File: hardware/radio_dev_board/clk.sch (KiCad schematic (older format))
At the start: 11 parts

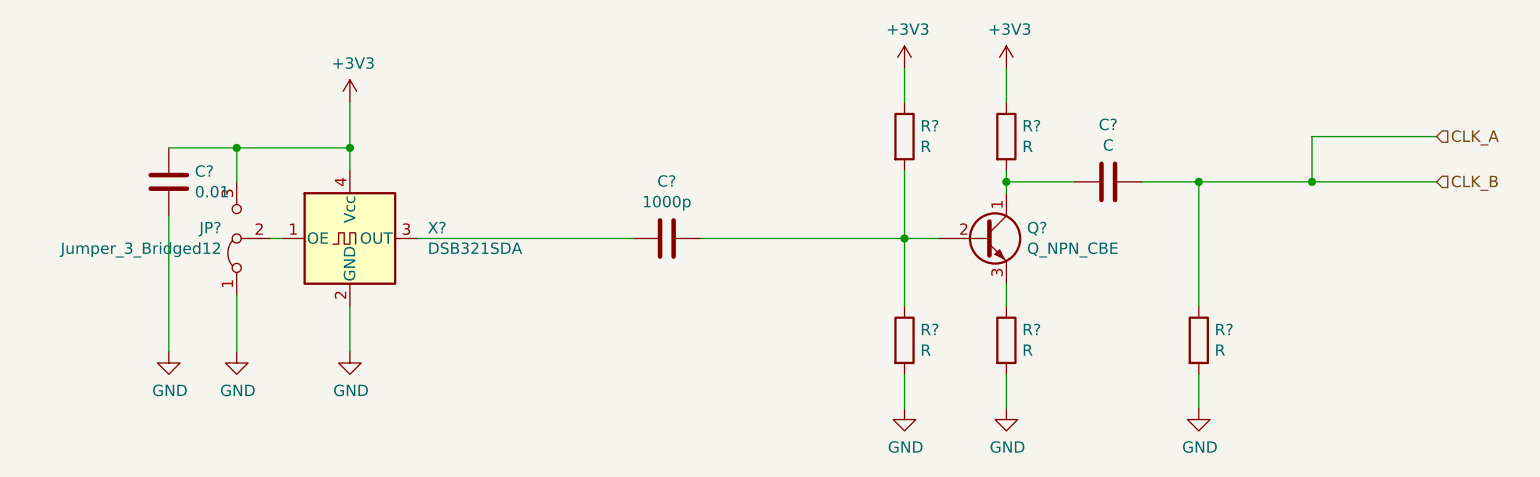
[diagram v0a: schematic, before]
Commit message: added radio USB serial channel. Update board layout
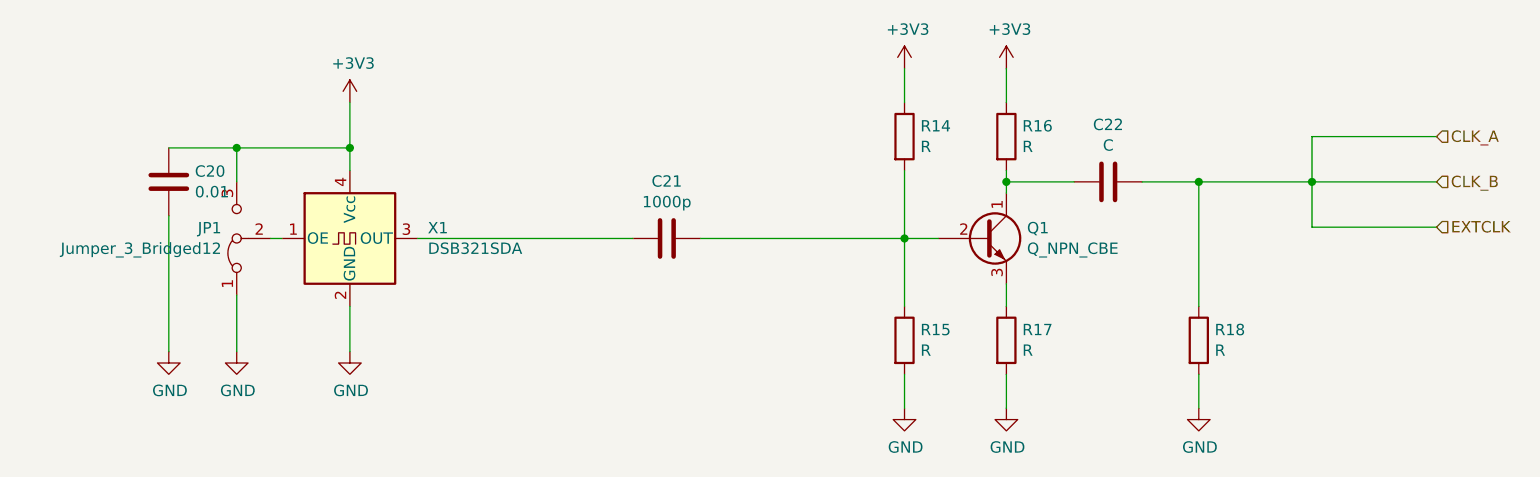
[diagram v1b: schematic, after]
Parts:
- C20, C21, C22: renamed from C?; footprint (none) -> Capacitor_SMD:C_0603_1608Metric_Pad1.05x0.95mm_HandSolder
- JP1: renamed from JP?; footprint (none) -> Jumper:SolderJumper-3_P1.3mm_Bridged2Bar12_Pad1.0x1.5mm
- Q1: renamed from Q?; footprint (none) -> Package_TO_SOT_SMD:SOT-23
- R14, R15, R16, R17, R18: renamed from R?; footprint (none) -> Resistor_SMD:R_0603_1608Metric_Pad1.05x0.95mm_HandSolder
- gave numbers to parts that had none: 1
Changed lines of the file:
@@
 $Descr A4 11693 8268
 encoding utf-8
-Sheet 5 5
+Sheet 5 6
 Title ""
 Date ""
@@
 $EndDescr
 $Comp
-L Oscillator:SG-210SED X?
+L Oscillator:SG-210SED X1
 U 1 1 5DEE1FC3
 P 4550 4050
-F 0 "X?" H 4894 4096 50  0000 L CNN
+F 0 "X1" H 4894 4096 50  0000 L CNN
 F 1 "DSB321SDA" H 4894 4005 50  0000 L CNN
 F 2 "Oscillator:Oscillator_SMD_SeikoEpson_SG210-4Pin_2.5x2.0mm" H 5000 3700 50  0001 C CNN
@@
 $EndComp
 $Comp
-L power:+3V3 #PWR?
+L power:+3V3 #PWR060
 U 1 1 5DEE2566
 P 4550 3450
-F 0 "#PWR?" H 4550 3300 50  0001 C CNN
+F 0 "#PWR060" H 4550 3300 50  0001 C CNN
 F 1 "+3V3" H 4565 3623 50  0000 C CNN
 F 2 "" H 4550 3450 50  0001 C CNN
@@
 $EndComp
 $Comp
-L power:GND #PWR?
+L power:GND #PWR061
 U 1 1 5DEE2C97
 P 4550 4550
-F 0 "#PWR?" H 4550 4300 50  0001 C CNN
+F 0 "#PWR061" H 4550 4300 50  0001 C CNN
 F 1 "GND" H 4555 4377 50  0000 C CNN
 F 2 "" H 4550 4550 50  0001 C CNN
@@
 $EndComp
 $Comp
-L power:GND #PWR?
+L power:GND #PWR059
 U 1 1 5DEE2E7E
 P 4050 4550
-F 0 "#PWR?" H 4050 4300 50  0001 C CNN
+F 0 "#PWR059" H 4050 4300 50  0001 C CNN
 F 1 "GND" H 4055 4377 50  0000 C CNN
 F 2 "" H 4050 4550 50  0001 C CNN
@@
 	4850 4050 5800 4050
 $Comp
-L Device:C C?
+L Device:C C21
 U 1 1 5DEE3315
 P 5950 4050
-F 0 "C?" V 5698 4050 50  0000 C CNN
+F 0 "C21" V 5698 4050 50  0000 C CNN
 F 1 "1000p" V 5789 4050 50  0000 C CNN
-F 2 "" H 5988 3900 50  0001 C CNN
+F 2 "Capacitor_SMD:C_0603_1608Metric_Pad1.05x0.95mm_HandSolder" H 5988 3900 50  0001 C CNN
 F 3 "~" H 5950 4050 50  0001 C CNN
 	1    5950 4050
@@
 $EndComp
 $Comp
-L Device:C C?
+L Device:C C20
 U 1 1 5DEE35E3
 P 3750 3800
-F 0 "C?" H 3865 3846 50  0000 L CNN
+F 0 "C20" H 3865 3846 50  0000 L CNN
 F 1 "0.01" H 3865 3755 50  0000 L CNN
-F 2 "" H 3788 3650 50  0001 C CNN
+F 2 "Capacitor_SMD:C_0603_1608Metric_Pad1.05x0.95mm_HandSolder" H 3788 3650 50  0001 C CNN
 F 3 "~" H 3750 3800 50  0001 C CNN
 	1    3750 3800
@@
 $EndComp
 $Comp
-L power:GND #PWR?
+L power:GND #PWR058
 U 1 1 5DEE3829
 P 3750 4550
-F 0 "#PWR?" H 3750 4300 50  0001 C CNN
+F 0 "#PWR058" H 3750 4300 50  0001 C CNN
 F 1 "GND" H 3755 4377 50  0000 C CNN
 F 2 "" H 3750 4550 50  0001 C CNN
@@
 	4550 3650 4550 3750
 $Comp
-L Jumper:Jumper_3_Bridged12 JP?
+L Jumper:Jumper_3_Bridged12 JP1
 U 1 1 5DEE4B8B
 P 4050 4050
-F 0 "JP?" V 4096 4117 50  0000 L CNN
+F 0 "JP1" V 4096 4117 50  0000 L CNN
 F 1 "Jumper_3_Bridged12" V 4005 4117 50  0000 L CNN
-F 2 "" H 4050 4050 50  0001 C CNN
+F 2 "Jumper:SolderJumper-3_P1.3mm_Bridged2Bar12_Pad1.0x1.5mm" H 4050 4050 50  0001 C CNN
 F 3 "~" H 4050 4050 50  0001 C CNN
 	1    4050 4050
@@
 	4200 4050 4250 4050
 $Comp
-L Device:Q_NPN_CBE Q?
+L Device:Q_NPN_CBE Q1
 U 1 1 5DEE8696
 P 7350 4050
-F 0 "Q?" H 7541 4096 50  0000 L CNN
+F 0 "Q1" H 7541 4096 50  0000 L CNN
 F 1 "Q_NPN_CBE" H 7541 4005 50  0000 L CNN
-F 2 "" H 7550 4150 50  0001 C CNN
+F 2 "Package_TO_SOT_SMD:SOT-23" H 7550 4150 50  0001 C CNN
 F 3 "~" H 7350 4050 50  0001 C CNN
 	1    7350 4050
@@
 $EndComp
 $Comp
-L Device:R R?
+L Device:R R14
 U 1 1 5DEE8AFA
 P 7000 3600
-F 0 "R?" H 7070 3646 50  0000 L CNN
+F 0 "R14" H 7070 3646 50  0000 L CNN
 F 1 "R" H 7070 3555 50  0000 L CNN
-F 2 "" V 6930 3600 50  0001 C CNN
+F 2 "Resistor_SMD:R_0603_1608Metric_Pad1.05x0.95mm_HandSolder" V 6930 3600 50  0001 C CNN
 F 3 "~" H 7000 3600 50  0001 C CNN
 	1    7000 3600
@@
 $EndComp
 $Comp
-L Device:R R?
+L Device:R R15
 U 1 1 5DEE8CDD
 P 7000 4500
-F 0 "R?" H 7070 4546 50  0000 L CNN
+F 0 "R15" H 7070 4546 50  0000 L CNN
 F 1 "R" H 7070 4455 50  0000 L CNN
-F 2 "" V 6930 4500 50  0001 C CNN
+F 2 "Resistor_SMD:R_0603_1608Metric_Pad1.05x0.95mm_HandSolder" V 6930 4500 50  0001 C CNN
 F 3 "~" H 7000 4500 50  0001 C CNN
 	1    7000 4500
@@
 $EndComp
 $Comp
-L power:GND #PWR?
+L power:GND #PWR063
 U 1 1 5DEE901E
 P 7000 4800
-F 0 "#PWR?" H 7000 4550 50  0001 C CNN
+F 0 "#PWR063" H 7000 4550 50  0001 C CNN
 F 1 "GND" H 7005 4627 50  0000 C CNN
 F 2 "" H 7000 4800 50  0001 C CNN
@@
 $EndComp
 $Comp
-L power:+3V3 #PWR?
+L power:+3V3 #PWR062
 U 1 1 5DEE9234
 P 7000 3300
-F 0 "#PWR?" H 7000 3150 50  0001 C CNN
+F 0 "#PWR062" H 7000 3150 50  0001 C CNN
 F 1 "+3V3" H 7015 3473 50  0000 C CNN
 F 2 "" H 7000 3300 50  0001 C CNN
@@
 $EndComp
 $Comp
-L Device:R R?
+L Device:R R16
 U 1 1 5DEE9973
 P 7450 3600
-F 0 "R?" H 7520 3646 50  0000 L CNN
+F 0 "R16" H 7520 3646 50  0000 L CNN
 F 1 "R" H 7520 3555 50  0000 L CNN
-F 2 "" V 7380 3600 50  0001 C CNN
+F 2 "Resistor_SMD:R_0603_1608Metric_Pad1.05x0.95mm_HandSolder" V 7380 3600 50  0001 C CNN
 F 3 "~" H 7450 3600 50  0001 C CNN
 	1    7450 3600
@@
 $EndComp
 $Comp
-L power:+3V3 #PWR?
+L power:+3V3 #PWR064
 U 1 1 5DEEA747
 P 7450 3300
-F 0 "#PWR?" H 7450 3150 50  0001 C CNN
+F 0 "#PWR064" H 7450 3150 50  0001 C CNN
 F 1 "+3V3" H 7465 3473 50  0000 C CNN
 F 2 "" H 7450 3300 50  0001 C CNN
@@
 $EndComp
 $Comp
-L Device:R R?
+L Device:R R17
 U 1 1 5DEEB87E
 P 7450 4500
-F 0 "R?" H 7520 4546 50  0000 L CNN
+F 0 "R17" H 7520 4546 50  0000 L CNN
 F 1 "R" H 7520 4455 50  0000 L CNN
-F 2 "" V 7380 4500 50  0001 C CNN
+F 2 "Resistor_SMD:R_0603_1608Metric_Pad1.05x0.95mm_HandSolder" V 7380 4500 50  0001 C CNN
 F 3 "~" H 7450 4500 50  0001 C CNN
 	1    7450 4500
@@
 $EndComp
 $Comp
-L power:GND #PWR?
+L power:GND #PWR065
 U 1 1 5DEEC8A7
 P 7450 4800
-F 0 "#PWR?" H 7450 4550 50  0001 C CNN
+F 0 "#PWR065" H 7450 4550 50  0001 C CNN
 F 1 "GND" H 7455 4627 50  0000 C CNN
 F 2 "" H 7450 4800 50  0001 C CNN
@@
 	7450 3450 7450 3300
 $Comp
-L Device:C C?
+L Device:C C22
 U 1 1 5DEF0359
 P 7900 3800
-F 0 "C?" V 7648 3800 50  0000 C CNN
+F 0 "C22" V 7648 3800 50  0000 C CNN
 F 1 "C" V 7739 3800 50  0000 C CNN
-F 2 "" H 7938 3650 50  0001 C CNN
+F 2 "Capacitor_SMD:C_0603_1608Metric_Pad1.05x0.95mm_HandSolder" H 7938 3650 50  0001 C CNN
 F 3 "~" H 7900 3800 50  0001 C CNN
 	1    7900 3800
@@
 	8050 3800 8300 3800
 $Comp
-L Device:R R?
+L Device:R R18
 U 1 1 5DEF2752
 P 8300 4500
-F 0 "R?" H 8370 4546 50  0000 L CNN
+F 0 "R18" H 8370 4546 50  0000 L CNN
 F 1 "R" H 8370 4455 50  0000 L CNN
-F 2 "" V 8230 4500 50  0001 C CNN
+F 2 "Resistor_SMD:R_0603_1608Metric_Pad1.05x0.95mm_HandSolder" V 8230 4500 50  0001 C CNN
 F 3 "~" H 8300 4500 50  0001 C CNN
 	1    8300 4500
@@
 $EndComp
 $Comp
-L power:GND #PWR?
+L power:GND #PWR066
 U 1 1 5DEF2E06
 P 8300 4800
-F 0 "#PWR?" H 8300 4550 50  0001 C CNN
+F 0 "#PWR066" H 8300 4550 50  0001 C CNN
 F 1 "GND" H 8305 4627 50  0000 C CNN
 F 2 "" H 8300 4800 50  0001 C CNN
@@
 Text HLabel 9350 3800 2    50   Input ~ 0
 CLK_B
+Wire Wire Line
+	8800 3800 8800 4000
+Wire Wire Line
+	8800 4000 9350 4000
+Text HLabel 9350 4000 2    50   Input ~ 0
+EXTCLK
 $EndSCHEMATC

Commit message: added program and misc buttons. Finish layout
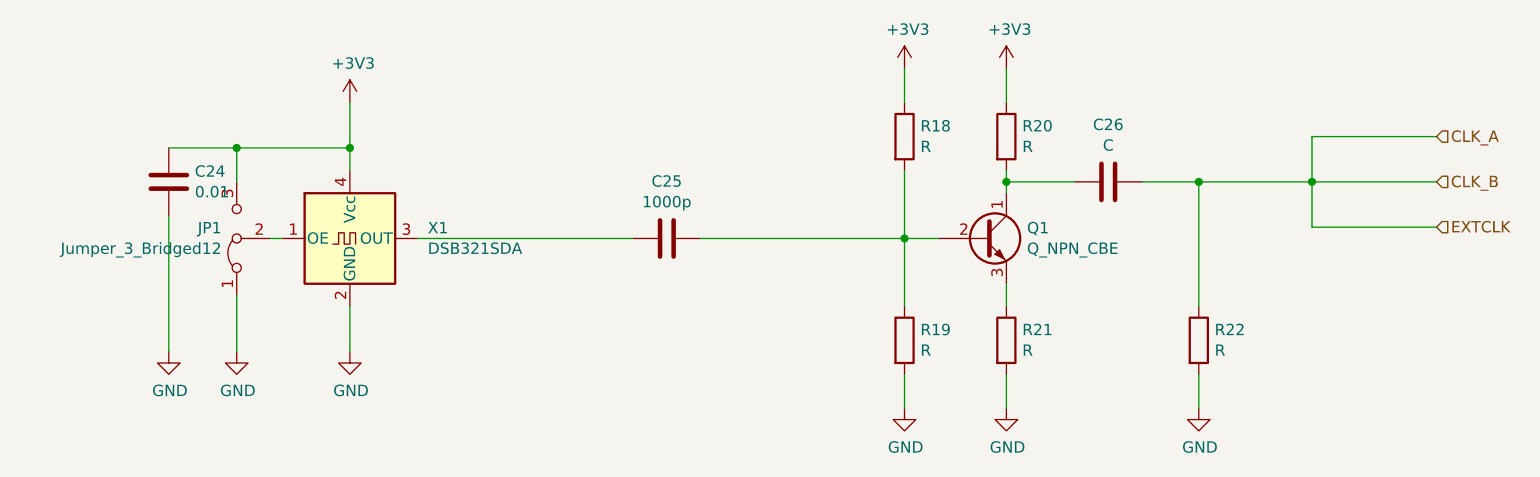
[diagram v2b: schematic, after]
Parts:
- renumbered C20 to C24, C21 to C25, C22 to C26, R14 to R18, R15 to R19, R16 to R20, R17 to R21, R18 to R22
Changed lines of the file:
@@
 $EndComp
 $Comp
-L power:+3V3 #PWR060
+L power:+3V3 #PWR071
 U 1 1 5DEE2566
 P 4550 3450
-F 0 "#PWR060" H 4550 3300 50  0001 C CNN
+F 0 "#PWR071" H 4550 3300 50  0001 C CNN
 F 1 "+3V3" H 4565 3623 50  0000 C CNN
 F 2 "" H 4550 3450 50  0001 C CNN
@@
 $EndComp
 $Comp
-L power:GND #PWR061
+L power:GND #PWR072
 U 1 1 5DEE2C97
 P 4550 4550
-F 0 "#PWR061" H 4550 4300 50  0001 C CNN
+F 0 "#PWR072" H 4550 4300 50  0001 C CNN
 F 1 "GND" H 4555 4377 50  0000 C CNN
 F 2 "" H 4550 4550 50  0001 C CNN
@@
 $EndComp
 $Comp
-L power:GND #PWR059
+L power:GND #PWR070
 U 1 1 5DEE2E7E
 P 4050 4550
-F 0 "#PWR059" H 4050 4300 50  0001 C CNN
+F 0 "#PWR070" H 4050 4300 50  0001 C CNN
 F 1 "GND" H 4055 4377 50  0000 C CNN
 F 2 "" H 4050 4550 50  0001 C CNN
@@
 	4850 4050 5800 4050
 $Comp
-L Device:C C21
+L Device:C C25
 U 1 1 5DEE3315
 P 5950 4050
-F 0 "C21" V 5698 4050 50  0000 C CNN
+F 0 "C25" V 5698 4050 50  0000 C CNN
 F 1 "1000p" V 5789 4050 50  0000 C CNN
 F 2 "Capacitor_SMD:C_0603_1608Metric_Pad1.05x0.95mm_HandSolder" H 5988 3900 50  0001 C CNN
@@
 $EndComp
 $Comp
-L Device:C C20
+L Device:C C24
 U 1 1 5DEE35E3
 P 3750 3800
-F 0 "C20" H 3865 3846 50  0000 L CNN
+F 0 "C24" H 3865 3846 50  0000 L CNN
 F 1 "0.01" H 3865 3755 50  0000 L CNN
 F 2 "Capacitor_SMD:C_0603_1608Metric_Pad1.05x0.95mm_HandSolder" H 3788 3650 50  0001 C CNN
@@
 $EndComp
 $Comp
-L power:GND #PWR058
+L power:GND #PWR069
 U 1 1 5DEE3829
 P 3750 4550
-F 0 "#PWR058" H 3750 4300 50  0001 C CNN
+F 0 "#PWR069" H 3750 4300 50  0001 C CNN
 F 1 "GND" H 3755 4377 50  0000 C CNN
 F 2 "" H 3750 4550 50  0001 C CNN
@@
 $EndComp
 $Comp
-L Device:R R14
+L Device:R R18
 U 1 1 5DEE8AFA
 P 7000 3600
-F 0 "R14" H 7070 3646 50  0000 L CNN
+F 0 "R18" H 7070 3646 50  0000 L CNN
 F 1 "R" H 7070 3555 50  0000 L CNN
 F 2 "Resistor_SMD:R_0603_1608Metric_Pad1.05x0.95mm_HandSolder" V 6930 3600 50  0001 C CNN
@@
 $EndComp
 $Comp
-L Device:R R15
+L Device:R R19
 U 1 1 5DEE8CDD
 P 7000 4500
-F 0 "R15" H 7070 4546 50  0000 L CNN
+F 0 "R19" H 7070 4546 50  0000 L CNN
 F 1 "R" H 7070 4455 50  0000 L CNN
 F 2 "Resistor_SMD:R_0603_1608Metric_Pad1.05x0.95mm_HandSolder" V 6930 4500 50  0001 C CNN
@@
 $EndComp
 $Comp
-L power:GND #PWR063
+L power:GND #PWR074
 U 1 1 5DEE901E
 P 7000 4800
-F 0 "#PWR063" H 7000 4550 50  0001 C CNN
+F 0 "#PWR074" H 7000 4550 50  0001 C CNN
 F 1 "GND" H 7005 4627 50  0000 C CNN
 F 2 "" H 7000 4800 50  0001 C CNN
@@
 $EndComp
 $Comp
-L power:+3V3 #PWR062
+L power:+3V3 #PWR073
 U 1 1 5DEE9234
 P 7000 3300
-F 0 "#PWR062" H 7000 3150 50  0001 C CNN
+F 0 "#PWR073" H 7000 3150 50  0001 C CNN
 F 1 "+3V3" H 7015 3473 50  0000 C CNN
 F 2 "" H 7000 3300 50  0001 C CNN
@@
 $EndComp
 $Comp
-L Device:R R16
+L Device:R R20
 U 1 1 5DEE9973
 P 7450 3600
-F 0 "R16" H 7520 3646 50  0000 L CNN
+F 0 "R20" H 7520 3646 50  0000 L CNN
 F 1 "R" H 7520 3555 50  0000 L CNN
 F 2 "Resistor_SMD:R_0603_1608Metric_Pad1.05x0.95mm_HandSolder" V 7380 3600 50  0001 C CNN
@@
 $EndComp
 $Comp
-L power:+3V3 #PWR064
+L power:+3V3 #PWR075
 U 1 1 5DEEA747
 P 7450 3300
-F 0 "#PWR064" H 7450 3150 50  0001 C CNN
+F 0 "#PWR075" H 7450 3150 50  0001 C CNN
 F 1 "+3V3" H 7465 3473 50  0000 C CNN
 F 2 "" H 7450 3300 50  0001 C CNN
@@
 $EndComp
 $Comp
-L Device:R R17
+L Device:R R21
 U 1 1 5DEEB87E
 P 7450 4500
-F 0 "R17" H 7520 4546 50  0000 L CNN
+F 0 "R21" H 7520 4546 50  0000 L CNN
 F 1 "R" H 7520 4455 50  0000 L CNN
 F 2 "Resistor_SMD:R_0603_1608Metric_Pad1.05x0.95mm_HandSolder" V 7380 4500 50  0001 C CNN
@@
 $EndComp
 $Comp
-L power:GND #PWR065
+L power:GND #PWR076
 U 1 1 5DEEC8A7
 P 7450 4800
-F 0 "#PWR065" H 7450 4550 50  0001 C CNN
+F 0 "#PWR076" H 7450 4550 50  0001 C CNN
 F 1 "GND" H 7455 4627 50  0000 C CNN
 F 2 "" H 7450 4800 50  0001 C CNN
@@
 	7450 3450 7450 3300
 $Comp
-L Device:C C22
+L Device:C C26
 U 1 1 5DEF0359
 P 7900 3800
-F 0 "C22" V 7648 3800 50  0000 C CNN
+F 0 "C26" V 7648 3800 50  0000 C CNN
 F 1 "C" V 7739 3800 50  0000 C CNN
 F 2 "Capacitor_SMD:C_0603_1608Metric_Pad1.05x0.95mm_HandSolder" H 7938 3650 50  0001 C CNN
@@
 	8050 3800 8300 3800
 $Comp
-L Device:R R18
+L Device:R R22
 U 1 1 5DEF2752
 P 8300 4500
-F 0 "R18" H 8370 4546 50  0000 L CNN
+F 0 "R22" H 8370 4546 50  0000 L CNN
 F 1 "R" H 8370 4455 50  0000 L CNN
 F 2 "Resistor_SMD:R_0603_1608Metric_Pad1.05x0.95mm_HandSolder" V 8230 4500 50  0001 C CNN
@@
 $EndComp
 $Comp
-L power:GND #PWR066
+L power:GND #PWR077
 U 1 1 5DEF2E06
 P 8300 4800
-F 0 "#PWR066" H 8300 4550 50  0001 C CNN
+F 0 "#PWR077" H 8300 4550 50  0001 C CNN
 F 1 "GND" H 8305 4627 50  0000 C CNN
 F 2 "" H 8300 4800 50  0001 C CNN
